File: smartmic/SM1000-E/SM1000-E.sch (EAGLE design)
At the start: 199 parts, among them CN1 HDR100-3, CN10 ST-3509, CN11 HDR100-3, CN12 HRS-A3C-16DA, CN13 CONN-BOOM-XH-2A, CN2 JS-MU3-002, CN3 DS-0518, CN4 RJ-45, CN5 ST-3509, CN6 ST-3509, CN7 ST-3509, CN8 ST-3509, CN9 ST-3509, J1 JMP-2PIN, J3 JMP-2PIN, J4 JMP-2PIN, P1 TPAD50, P10 TPAD50, P11 TPAD50, P12 TPAD50, P13 TPAD50, P14 TPAD50, P16 TPAD50, P18 TPAD50, P19 TPAD50, P2 TPAD50, P20 TPAD50, P3 TPAD50, P4 TPAD50, P5 TPAD50, P6 TPAD50, P7 TPAD50, P8 TPAD50, P9 TPAD50, SW1 SW-SPDT-8US8WR2C2M7RES, SW2 TS-026, SW3 DPDT, SW4 TS-026, SW5 TS-02B, SW6 SW-LC2259, SW7 SW-LC2259, T1 SM-LP-5001, T2 SM-LP-5001, U1 STM32F405VGT6, U2 LD3985M33R, U3 STMPS2141, U4 EMIF02-USB03F2, U5 TPS54329E, U6 LMV341, U7 LMV341, U8 LM386M-1, U9 LMV341

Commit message: IMPLEMENT CHANGES PER SM1000-E-CHANGE-LOG.TXT RGB
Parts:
- removed CN13: CONN-BOOM-XH-2A, _RoweTel:CONN-BOOM-XH-2A
- removed SW6, SW7: SW-LC2259, _RoweTel:SW-LC2259
- J4: value JMP-2PIN -> CONN-BOOM-XH-2A; device _Coherix:JMP-2PIN -> _RoweTel:CONN-BOOM-XH-2A
- LED1: value LED-RED,RA -> LTST-S220KGKT
- LED2: value LED-RED,RA -> LTST-S220KRKT
- LED3: value LED-GRN,RA -> LTST-S220KGKT
- LED4: value LED-YEL,RA -> LTST-S220KRKT
- SW1: value SW-SPDT-8US8WR2C2M7RES -> SW-LC2259; device _RoweTel:SW-SPDT-8US8WR2C2M7RES -> _RoweTel:SW-LC2259
- SW3: value DPDT -> SW-LC2259EENP; device _RoweTel:SW-PWR-E-SWITCH -> _RoweTel:SW-LC2259
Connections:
- net +VIN: now also SW3.1, SW3.4; no longer SW3.3, SW3.6
- net GND: now also J4.1, SW1.7, SW1.8, SW3.7, SW3.8; no longer J4.2, SW1.G1, SW1.G2
- net N$14: now also SW1.1
- net N$62: now also J4.2; no longer J4.1
- net VDD: now also SW1.2, SW1.5; no longer SW1.6
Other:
- note added: "05/19/15"
- note added: "05/20/15"
- note added: "CHANGE LED COLORS FOR LED1 , LED4"
- note added: "CHANGE PARTS SW1, SW3 & J4"
- note added: "DNL LED5,LED8 CIRCUITS"
- note added: "E"
- note added: "GREEN"
- note added: "RED"
- moved on the sheet: C1, C25, C46, C63, C70, LED1, LED2, LED3, LED4, R1, R12, R13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

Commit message: 21  [X]         From Mel: DNL LED5 and LED8 to save a little power. 			DNL LED8	RGB 			DNL R33 			DNL LED5 			DNL R17
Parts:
- LED5: value SML-LX0603SRW-TR -> SML-LX0603SRW
- LED8: value SML-LX0603SRW-TR -> DNL
- R17: value 1K,1% -> DNL
- R33: value 2.2K,1% -> DNL
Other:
- note added: "05/27/15"
- note added: "1K,1%"
- note added: "2.2K,1%"
- note added: "DNL"
- note added: "DNL LED5,R17,LED8,R33"
- note added: "LED,GREEN,RA"
- note added: "LED,RED,RA"
- note added: "NOTE: SEE PAGE 1 FOR CHANGES"
- note added: "SML-LX0603SRW-TR"
- note removed: "DNL LED5,LED8 CIRCUITS"
- note removed: "GREEN"
- note removed: "RED"
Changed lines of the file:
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@@
 <part name="V33" library="A-SUPPLY2" deviceset="GND" device=""/>
 <part name="V34" library="A-SUPPLY2" deviceset="GND" device=""/>
-<part name="R17" library="AA-ipc-7351-resistor" deviceset="RESISTOR_" device="0402" value="1K,1%"/>
+<part name="R17" library="AA-ipc-7351-resistor" deviceset="RESISTOR_" device="0402" value="DNL"/>
 <part name="V35" library="A-SUPPLY2" deviceset="GND" device=""/>
 <part name="U$2" library="A-SUPPLY2" deviceset="+3.3V" device=""/>
@@
 <part name="J3" library="_Coherix" deviceset="JMP-2PIN" device=""/>
 <part name="SH3" library="_Coherix" deviceset="SHUNT,0.1IN" device=""/>
-<part name="R33" library="AA-ipc-7351-resistor" deviceset="RESISTOR_" device="0402" value="2.2K,1%"/>
+<part name="R33" library="AA-ipc-7351-resistor" deviceset="RESISTOR_" device="0402" value="DNL"/>
 <part name="V58" library="A-SUPPLY2" deviceset="GND" device=""/>
 <part name="LD2" library="_RoweTel" deviceset="LTV-817S" device=""/>
@@
 <part name="CN3" library="_RoweTel" deviceset="DS-0518" device=""/>
 <part name="CN2" library="_RoweTel" deviceset="JS-MU3-002" device=""/>
-<part name="LED8" library="_RoweTel" deviceset="SML-LX0603SRW" device="" value="SML-LX0603SRW-TR"/>
-<part name="LED5" library="_RoweTel" deviceset="SML-LX0603SRW" device="" value="SML-LX0603SRW-TR"/>
+<part name="LED8" library="_RoweTel" deviceset="SML-LX0603SRW" device="" value="DNL"/>
+<part name="LED5" library="_RoweTel" deviceset="SML-LX0603SRW" device="" value=""/>
 <part name="SPKR1" library="_RoweTel" deviceset="SPKR-HY4004M-001" device=""/>
 <part name="SW3" library="_RoweTel" deviceset="SW-LC2259" device="" value="SW-LC2259EENP"/>
@@
 <text x="421.64" y="251.46" size="1.4224" layer="94" ratio="10">E</text>
 <text x="426.72" y="251.46" size="1.4224" layer="94" ratio="10">RGB</text>
-<text x="45.72" y="226.06" size="1.4224" layer="94" ratio="10">GREEN</text>
-<text x="45.72" y="205.74" size="1.4224" layer="94" ratio="10">GREEN</text>
-<text x="45.72" y="215.9" size="1.4224" layer="94" ratio="10">RED</text>
-<text x="45.72" y="195.58" size="1.4224" layer="94" ratio="10">RED</text>
+<text x="45.72" y="226.06" size="1.4224" layer="94" ratio="10">LED,GREEN,RA</text>
+<text x="45.72" y="205.74" size="1.4224" layer="94" ratio="10">LED,GREEN,RA</text>
+<text x="45.72" y="215.9" size="1.4224" layer="94" ratio="10">LED,RED,RA</text>
+<text x="45.72" y="195.58" size="1.4224" layer="94" ratio="10">LED,RED,RA</text>
 <text x="358.14" y="248.92" size="1.4224" layer="94" ratio="10">05/20/15</text>
 <text x="370.84" y="248.92" size="1.4224" layer="94" ratio="10">CHANGE LED COLORS FOR LED1 , LED4</text>
 <text x="421.64" y="248.92" size="1.4224" layer="94" ratio="10">E</text>
 <text x="426.72" y="248.92" size="1.4224" layer="94" ratio="10">RGB</text>
-<text x="358.14" y="246.38" size="1.4224" layer="94" ratio="10">05/20/15</text>
-<text x="370.84" y="246.38" size="1.4224" layer="94" ratio="10">DNL LED5,LED8 CIRCUITS</text>
+<text x="358.14" y="246.38" size="1.4224" layer="94" ratio="10">05/27/15</text>
+<text x="370.84" y="246.38" size="1.4224" layer="94" ratio="10">DNL LED5,R17,LED8,R33</text>
 <text x="421.64" y="246.38" size="1.4224" layer="94" ratio="10">E</text>
 <text x="426.72" y="246.38" size="1.4224" layer="94" ratio="10">RGB</text>
+<text x="289.56" y="144.78" size="1.4224" layer="94" ratio="10">1K,1%</text>
+<text x="289.56" y="129.54" size="1.4224" layer="94" ratio="10">SML-LX0603SRW-TR</text>
+<text x="289.56" y="132.08" size="1.4224" layer="96" ratio="10">DNL</text>
 </plain>
 <instances>
@@
 <text x="419.1" y="271.78" size="1.4224" layer="94" ratio="10">D</text>
 <text x="424.18" y="271.78" size="1.4224" layer="94" ratio="10">RGB</text>
-<text x="355.6" y="269.24" size="1.4224" layer="94" ratio="10">05/19/15</text>
-<text x="368.3" y="269.24" size="1.4224" layer="94" ratio="10">CHANGE PARTS SW1, SW3 &amp; J4</text>
-<text x="419.1" y="269.24" size="1.4224" layer="94" ratio="10">E</text>
-<text x="424.18" y="269.24" size="1.4224" layer="94" ratio="10">RGB</text>
+<text x="251.46" y="236.22" size="1.4224" layer="94" ratio="10">2.2K,1%</text>
+<text x="251.46" y="220.98" size="1.4224" layer="94" ratio="10">SML-LX0603SRW-TR</text>
+<text x="368.3" y="269.24" size="1.4224" layer="94" ratio="10">NOTE: SEE PAGE 1 FOR CHANGES</text>
 </plain>
 <instances>

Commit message: 4. [X] Add part outlines to layer tdoc for documentation.        Complete RGB
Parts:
- U3: device AA-IC:STMPS2141 -> _RoweTel:STMPS2141
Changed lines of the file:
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@@
 <part name="R28" library="AA-ipc-7351-resistor" deviceset="RESISTOR_" device="0402" value="22,1%"/>
 <part name="R30" library="AA-ipc-7351-resistor" deviceset="RESISTOR_" device="0603" value="0 Ohm"/>
-<part name="U3" library="AA-IC" deviceset="STMPS2141" device=""/>
+<part name="U3" library="_RoweTel" deviceset="STMPS2141" device=""/>
 <part name="V45" library="A-SUPPLY2" deviceset="+5V" device=""/>
 <part name="R25" library="AA-ipc-7351-resistor" deviceset="RESISTOR_" device="0402" value="10K,1%"/>

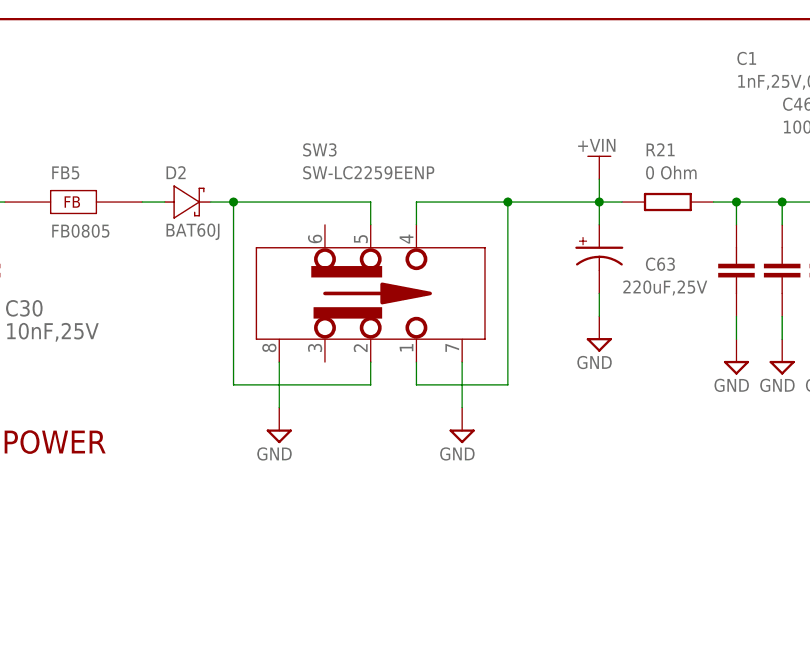
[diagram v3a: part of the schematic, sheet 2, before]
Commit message: Added schematic power switch SW3 wiring change(.pngs) to accomodate PCB routing. Updated SM1000-E-change-log.txt file to reflect update and comments on #27 RGB
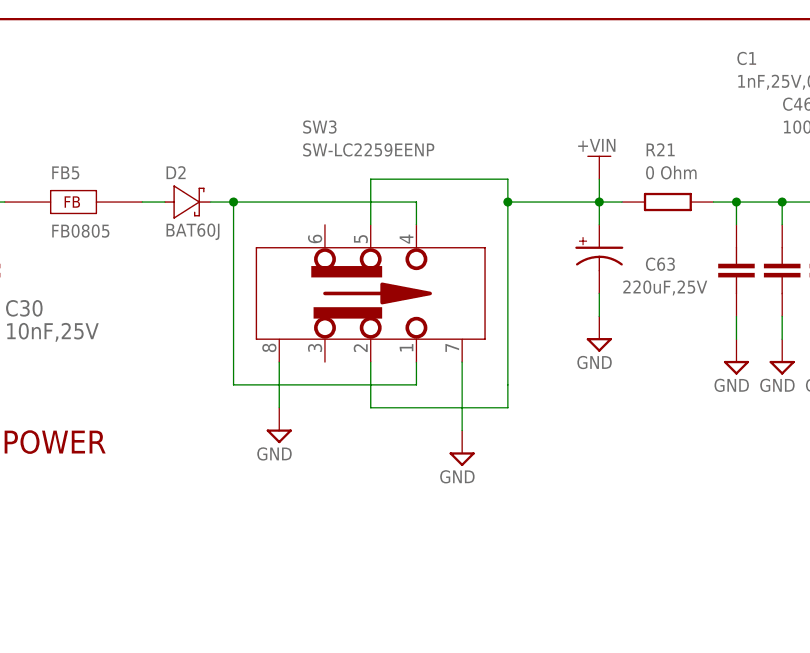
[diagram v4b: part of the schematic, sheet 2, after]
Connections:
- net +VIN: now also SW3.2, SW3.5; no longer SW3.1, SW3.4
- net N$81: now also SW3.1, SW3.4; no longer SW3.2, SW3.5
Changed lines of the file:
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@@
 </instance>
 <instance part="SW3" gate="G$1" x="86.36" y="248.92" smashed="yes">
-<attribute name="NAME" x="73.66" y="264.16" size="1.4224" layer="95" ratio="10"/>
-<attribute name="VALUE" x="73.66" y="261.62" size="1.4224" layer="95" ratio="10"/>
+<attribute name="NAME" x="73.66" y="266.7" size="1.4224" layer="95" ratio="10"/>
+<attribute name="VALUE" x="73.66" y="264.16" size="1.4224" layer="95" ratio="10"/>
 </instance>
 <instance part="J4" gate="G$1" x="111.76" y="45.72" smashed="yes" rot="R90">
@@
 <attribute name="VALUE" x="96.52" y="35.56" size="1.4224" layer="95" ratio="10"/>
 </instance>
-<instance part="V121" gate="GND" x="91.44" y="233.68" smashed="yes">
-<attribute name="VALUE" x="88.9" y="230.378" size="1.4224" layer="96" ratio="9"/>
+<instance part="V121" gate="GND" x="91.44" y="231.14" smashed="yes">
+<attribute name="VALUE" x="88.9" y="227.838" size="1.4224" layer="96" ratio="9"/>
 </instance>
 <instance part="V141" gate="GND" x="71.12" y="233.68" smashed="yes">
@@
 <segment>
 <pinref part="SW3" gate="G$1" pin="7"/>
-<wire x1="91.44" y1="241.3" x2="91.44" y2="236.22" width="0.1524" layer="91"/>
+<wire x1="91.44" y1="241.3" x2="91.44" y2="233.68" width="0.1524" layer="91"/>
 <pinref part="V121" gate="GND" pin="GND"/>
 </segment>
@@
 </segment>
 <segment>
-<wire x1="86.36" y1="259.08" x2="96.52" y2="259.08" width="0.1524" layer="91"/>
+<wire x1="96.52" y1="261.62" x2="96.52" y2="259.08" width="0.1524" layer="91"/>
 <pinref part="R21" gate="G$1" pin="1"/>
 <pinref part="C63" gate="G$1" pin="1"/>
@@
 <pinref part="U$1" gate="G$1" pin="+VIN"/>
 <wire x1="106.68" y1="261.62" x2="106.68" y2="259.08" width="0.1524" layer="91"/>
-<pinref part="SW3" gate="G$1" pin="4"/>
-<wire x1="86.36" y1="259.08" x2="86.36" y2="256.54" width="0.1524" layer="91"/>
 <junction x="96.52" y="259.08"/>
-<pinref part="SW3" gate="G$1" pin="1"/>
-<wire x1="86.36" y1="241.3" x2="86.36" y2="238.76" width="0.1524" layer="91"/>
-<wire x1="86.36" y1="238.76" x2="96.52" y2="238.76" width="0.1524" layer="91"/>
 <wire x1="96.52" y1="238.76" x2="96.52" y2="259.08" width="0.1524" layer="91"/>
+<wire x1="96.52" y1="261.62" x2="81.28" y2="261.62" width="0.1524" layer="91"/>
+<pinref part="SW3" gate="G$1" pin="5"/>
+<wire x1="81.28" y1="261.62" x2="81.28" y2="256.54" width="0.1524" layer="91"/>
+<pinref part="SW3" gate="G$1" pin="2"/>
+<wire x1="81.28" y1="241.3" x2="81.28" y2="236.22" width="0.1524" layer="91"/>
+<wire x1="81.28" y1="236.22" x2="96.52" y2="236.22" width="0.1524" layer="91"/>
+<wire x1="96.52" y1="236.22" x2="96.52" y2="238.76" width="0.1524" layer="91"/>
 </segment>
 </net>
@@
 <segment>
 <wire x1="81.28" y1="238.76" x2="66.04" y2="238.76" width="0.1524" layer="91"/>
-<pinref part="SW3" gate="G$1" pin="2"/>
-<wire x1="81.28" y1="241.3" x2="81.28" y2="238.76" width="0.1524" layer="91"/>
-<pinref part="SW3" gate="G$1" pin="5"/>
-<wire x1="81.28" y1="259.08" x2="81.28" y2="256.54" width="0.1524" layer="91"/>
 <wire x1="66.04" y1="259.08" x2="81.28" y2="259.08" width="0.1524" layer="91"/>
 <pinref part="D2" gate="G$1" pin="C"/>
@@
 <wire x1="66.04" y1="238.76" x2="66.04" y2="259.08" width="0.1524" layer="91"/>
 <junction x="66.04" y="259.08"/>
-</segment>
-</net>
+<pinref part="SW3" gate="G$1" pin="4"/>
+<wire x1="81.28" y1="259.08" x2="86.36" y2="259.08" width="0.1524" layer="91"/>
+<wire x1="86.36" y1="259.08" x2="86.36" y2="256.54" width="0.1524" layer="91"/>
+<wire x1="81.28" y1="238.76" x2="86.36" y2="238.76" width="0.1524" layer="91"/>
+<pinref part="SW3" gate="G$1" pin="1"/>
+<wire x1="86.36" y1="238.76" x2="86.36" y2="241.3" width="0.1524" layer="91"/>
+</segment>
+</net>

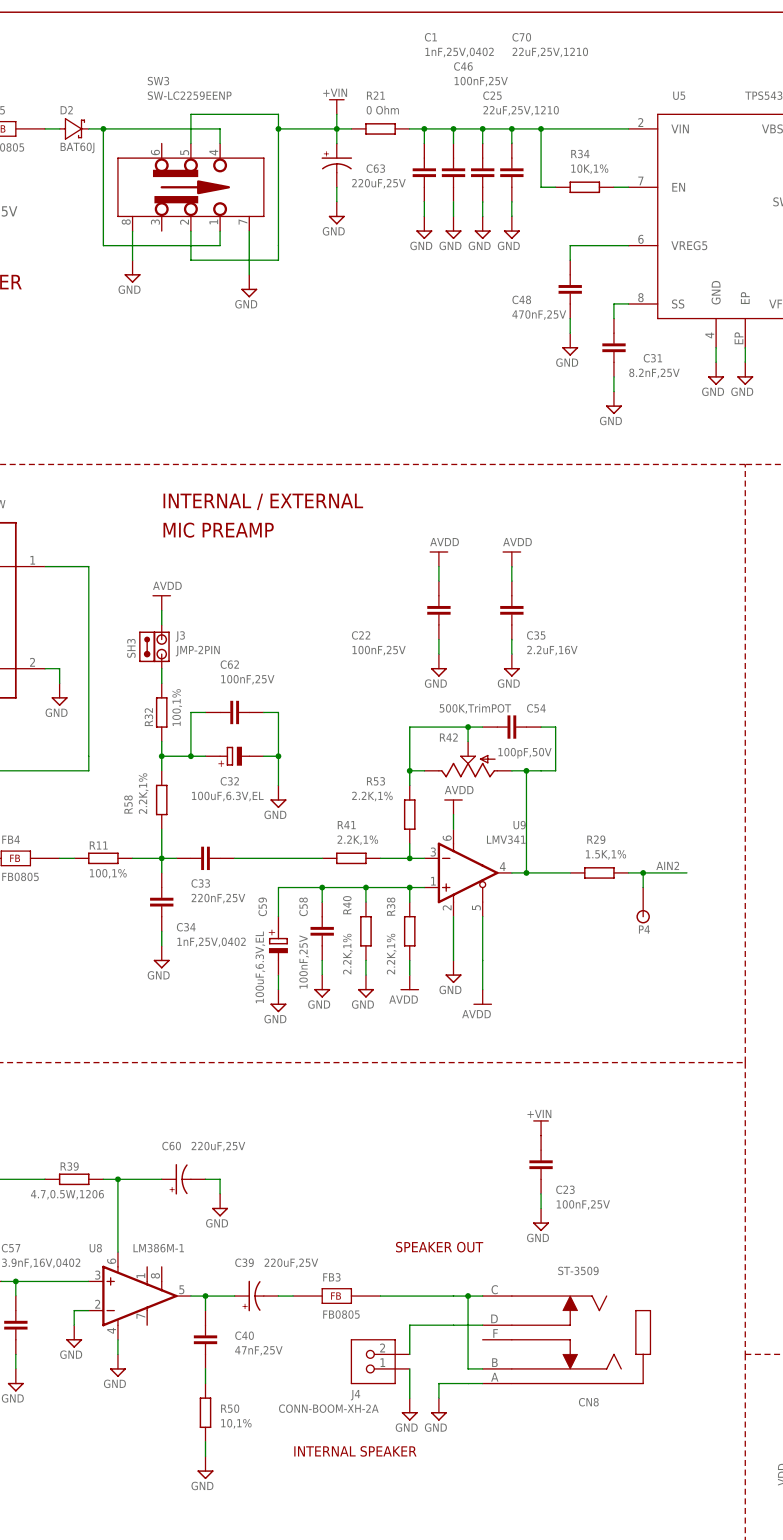
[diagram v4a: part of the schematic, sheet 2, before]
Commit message: Added jmpr mono ext speaker situation. Update SM1000-E-change-log file. RGB
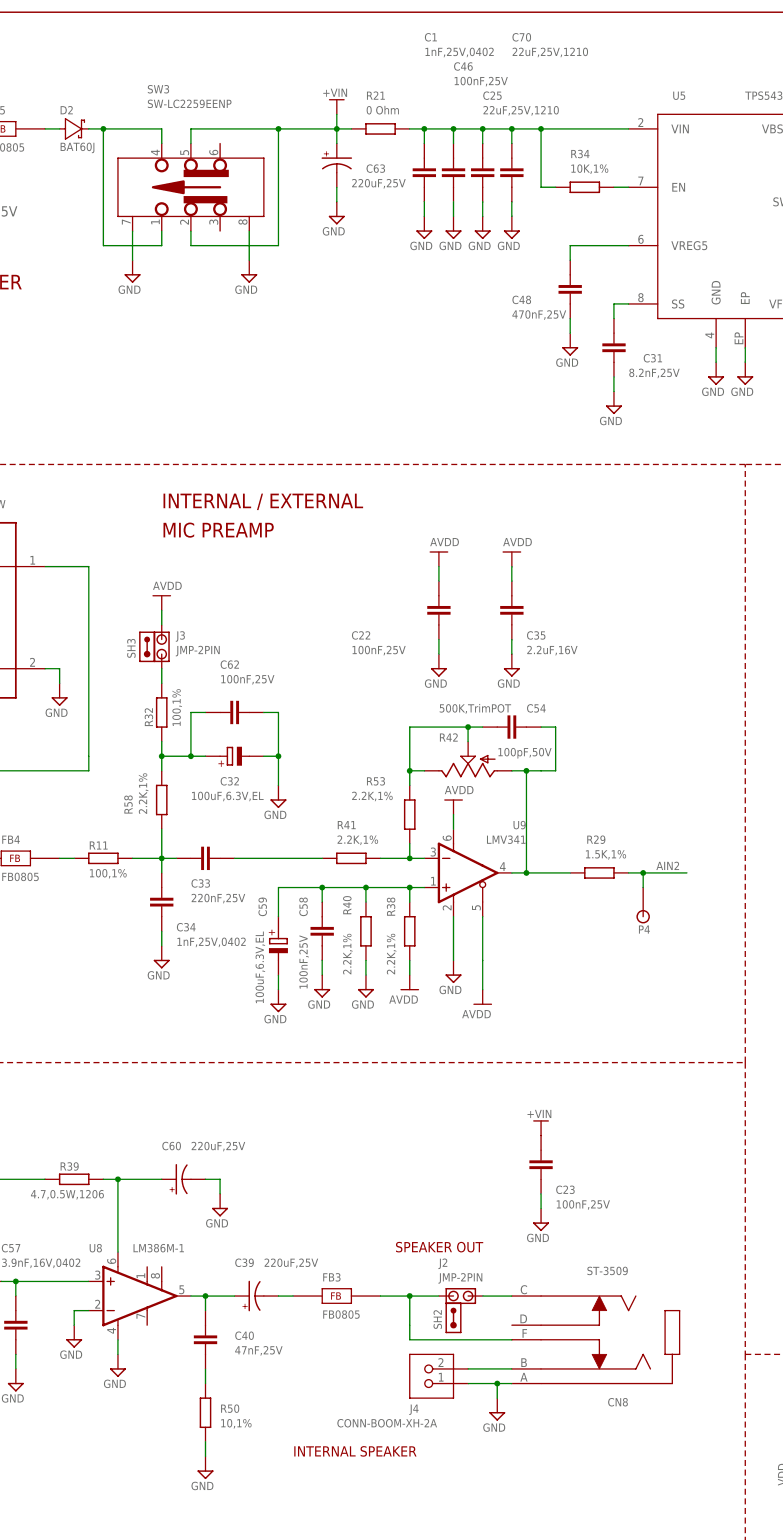
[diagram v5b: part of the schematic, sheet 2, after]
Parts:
- added J2: JMP-2PIN, _Coherix:JMP-2PIN
- added SH2: SHUNT,0.1IN, _Coherix:SHUNT,0.1IN
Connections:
- new net N$83: CN8.B, J4.2
- net N$62: now also CN8.E, FB3.2, J2.2; no longer CN8.D, J4.2
- net N$75: now also J2.1; no longer CN8.B, FB3.2
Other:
- moved on the sheet: CN8, J4
